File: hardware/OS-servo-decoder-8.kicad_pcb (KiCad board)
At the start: 2 copper layers, 41 x 74.5 mm, 59 parts, among them J1001 Conn_02x03_Odd_Even, J101 Screw_Terminal_01x04, J201 ICSP, J701 Conn_02x03_Odd_Even, J801 Conn_02x03_Odd_Even, J901 Conn_02x03_Odd_Even, SW601 SW_Push, SW602 SW_Push, SW603 SW_Push, SW604 SW_Push, SW605 SW_Push, U1001 6N137, U202 ATmega328-A, U901 MT2499A, Y201 Crystal_GND2

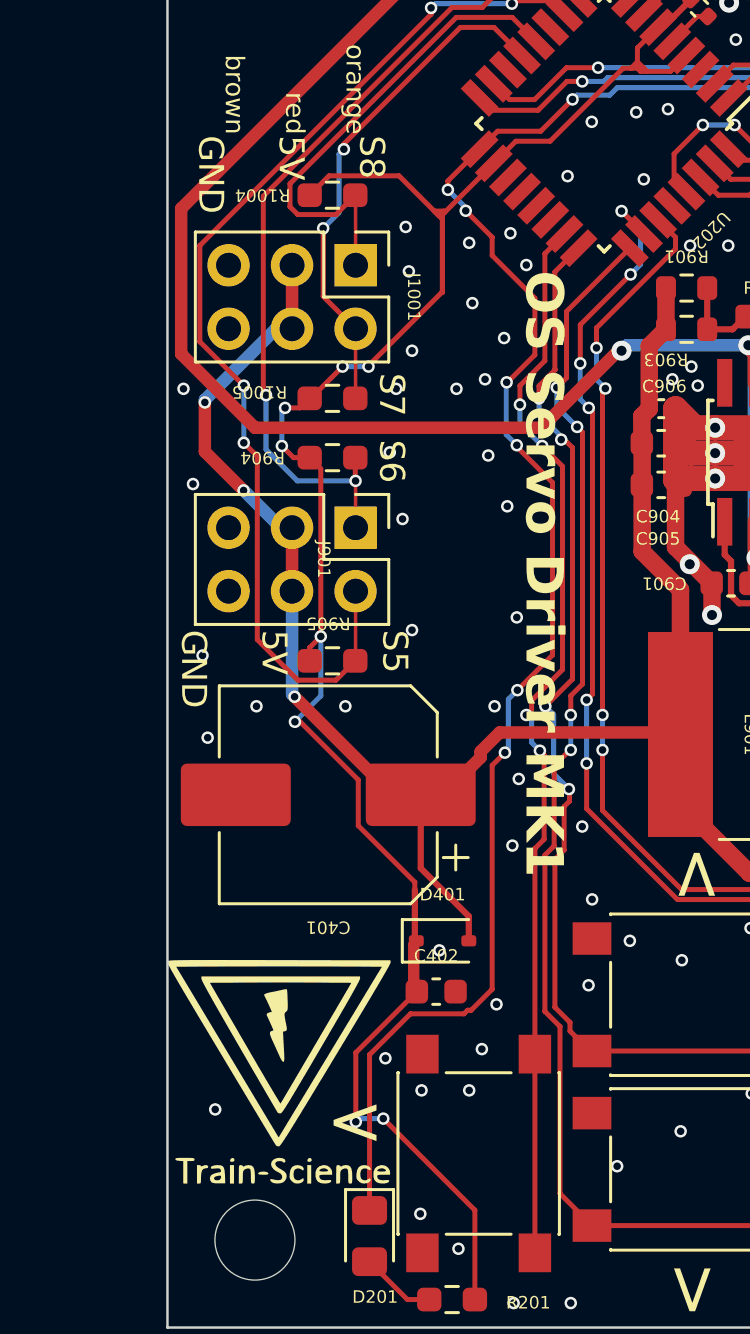
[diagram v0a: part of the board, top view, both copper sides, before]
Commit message: deleted source code in favor of sub module
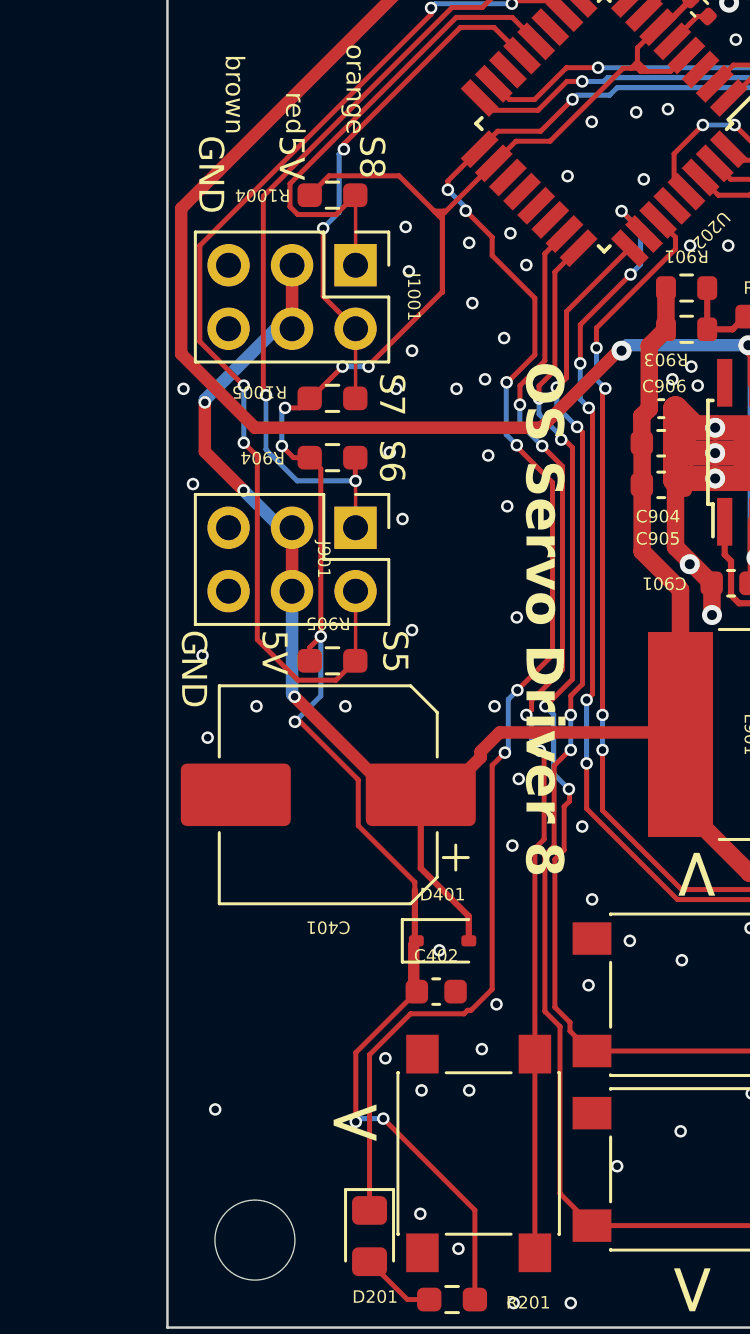
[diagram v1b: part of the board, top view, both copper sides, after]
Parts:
- removed G*** (x2): LOGO, custom_kicad_lib_sk:Train-Science logo small
- removed G***: LOGO, custom_kicad_lib_sk:servoDriverQR
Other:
- board text added: "OS Servo Driver 8"
- board text removed: "OS Servo Driver MK1"

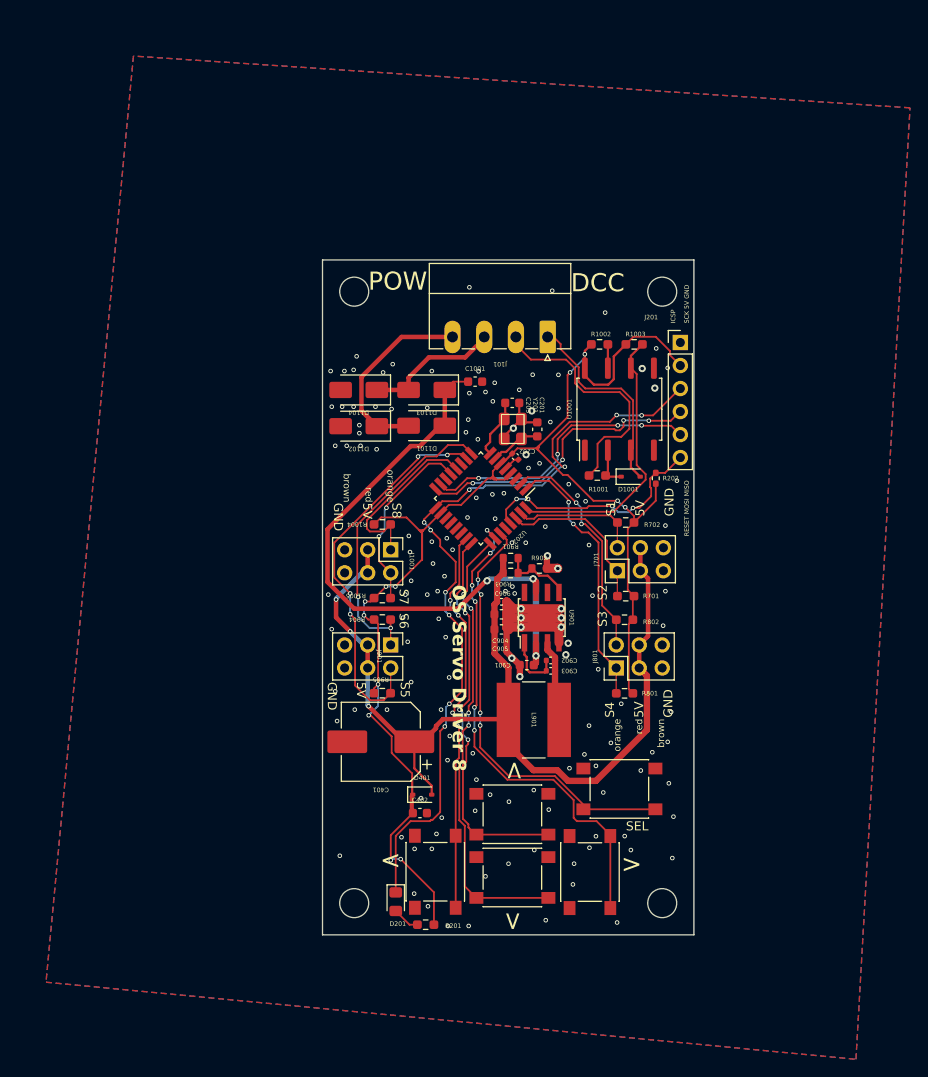
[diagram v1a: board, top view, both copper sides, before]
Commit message: update board file, made similar to OS solenoid decoder
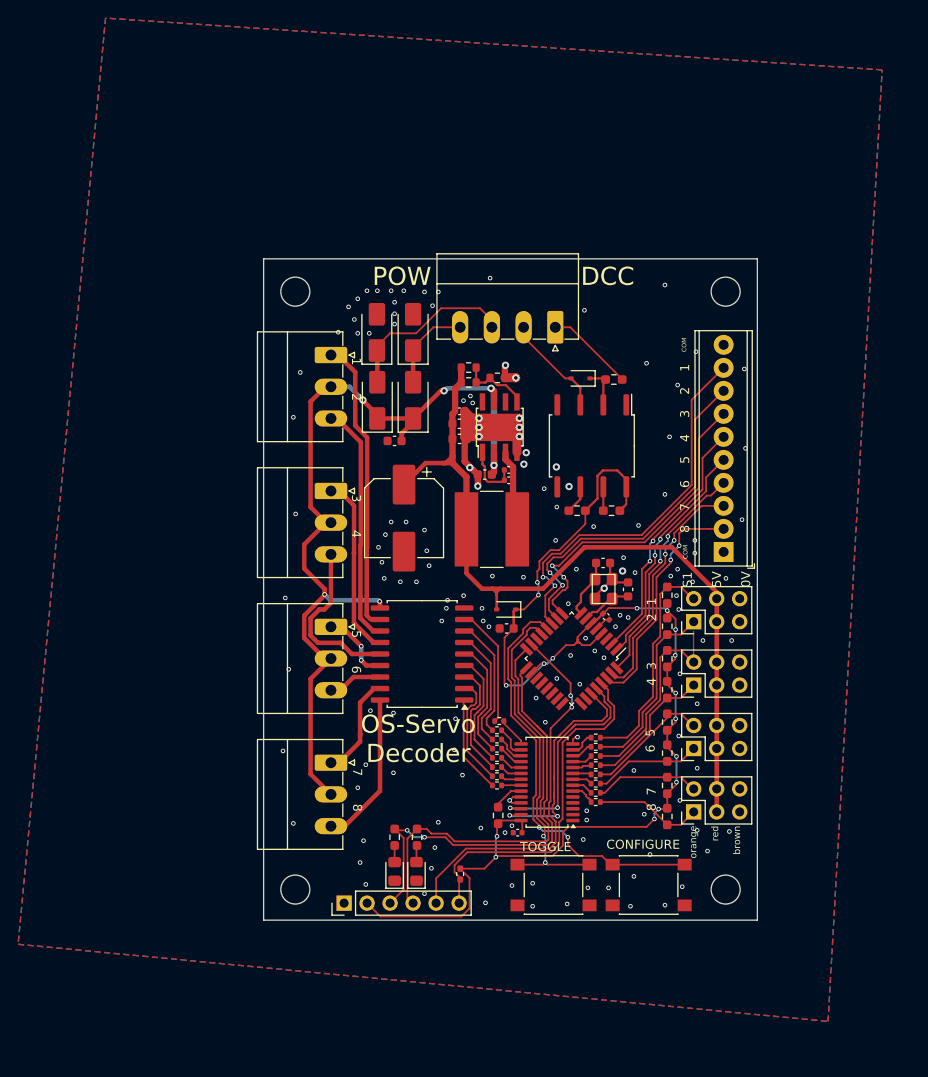
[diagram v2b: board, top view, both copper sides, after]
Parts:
- removed C1001: 100nF, Capacitor_SMD:C_0603_1608Metric
- removed the REF** at (104.0, 172.5)
- removed the REF** at (138.0, 172.5)
- removed the REF** at (138.0, 105.0)
- removed the REF** at (104.0, 105.0)
- removed the REF** at (120.9, 158.5)
- removed SW603, SW604, SW605: SW_Push, custom_kicad_lib_sk:tactile_SMD_6mm
- added C1601: 100nF, Capacitor_SMD:C_0402_1005Metric, F.Cu at (122.0, 164.7)
- added C501: 100nF, Capacitor_SMD:C_0603_1608Metric, F.Cu at (108.5, 121.5)
- added D202: LED, LED_SMD:LED_0805_2012Metric_Pad1.15x1.40mm_HandSolder, F.Cu at (110.9, 169.0)
- added G***: LOGO, custom_kicad_lib_sk:OS-model-railway-electronics-30mm, B.Cu at (121.3, 139.2)
- added J1301: Screw_Terminal_01x03, Connector_Phoenix_MC:PhoenixContact_MC_1,5_3-G-3.5_1x03_P3.50mm_Horizontal, F.Cu at (101.4, 112.0)
- added J1401: Screw_Terminal_01x03, Connector_Phoenix_MC:PhoenixContact_MC_1,5_3-G-3.5_1x03_P3.50mm_Horizontal, F.Cu at (101.4, 142.0)
- added J1501: Screw_Terminal_01x03, Connector_Phoenix_MC:PhoenixContact_MC_1,5_3-G-3.5_1x03_P3.50mm_Horizontal, F.Cu at (101.4, 157.0)
- added J401: Screw_Terminal_01x03, Connector_Phoenix_MC:PhoenixContact_MC_1,5_3-G-3.5_1x03_P3.50mm_Horizontal, F.Cu at (101.4, 127.0)
- added J501: Screw_Terminal_01x10, TerminalBlock_Phoenix:TerminalBlock_Phoenix_MPT-0,5-10-2.54_1x10_P2.54mm_Horizontal, F.Cu at (144.8, 133.7)
- added R1601: 10k, custom_kicad_lib_sk:R_0603_smalltext, F.Cu at (119.9, 162.8)
- added R1602: 220R, Resistor_SMD:R_0402_1005Metric, F.Cu at (130.7, 161.3)
- added R1603: 220R, Resistor_SMD:R_0402_1005Metric, F.Cu at (130.7, 160.3)
- added R1604: 220R, Resistor_SMD:R_0402_1005Metric, F.Cu at (130.7, 159.3)
- added R1605: 220R, Resistor_SMD:R_0402_1005Metric, F.Cu at (130.7, 158.3)
- added R1606: 220R, Resistor_SMD:R_0402_1005Metric, F.Cu at (130.7, 157.3)
- added R1607: 220R, Resistor_SMD:R_0402_1005Metric, F.Cu at (130.7, 156.3)
- added R1608: 220R, Resistor_SMD:R_0402_1005Metric, F.Cu at (130.7, 155.2)
- added R1609: 220R, Resistor_SMD:R_0402_1005Metric, F.Cu at (130.7, 154.2)
- added R1610: 220R, Resistor_SMD:R_0402_1005Metric, F.Cu at (120.0, 152.4)
- added R1611: 220R, Resistor_SMD:R_0402_1005Metric, F.Cu at (119.8, 153.4)
- added R1612: 220R, Resistor_SMD:R_0402_1005Metric, F.Cu at (119.8, 154.4)
- added R1613: 220R, Resistor_SMD:R_0402_1005Metric, F.Cu at (119.8, 155.4)
- added R1614: 220R, Resistor_SMD:R_0402_1005Metric, F.Cu at (119.8, 156.5)
- added R1615: 220R, Resistor_SMD:R_0402_1005Metric, F.Cu at (119.8, 157.5)
- added R1616: 220R, Resistor_SMD:R_0402_1005Metric, F.Cu at (119.8, 158.5)
- added R1617: 220R, Resistor_SMD:R_0402_1005Metric, F.Cu at (119.8, 159.5)
- added R203: 6k2, Resistor_SMD:R_0603_1608Metric_Pad0.98x0.95mm_HandSolder, F.Cu at (110.9, 165.2)
- added REF**: MountingHole_3.2mm_M3, MountingHole:MountingHole_3.2mm_M3, F.Cu at (145.0, 171.0)
- added REF**: MountingHole_3.2mm_M3, MountingHole:MountingHole_3.2mm_M3, F.Cu at (97.5, 105.0)
- added REF**: MountingHole_3.2mm_M3, MountingHole:MountingHole_3.2mm_M3, F.Cu at (97.5, 171.0)
- added REF**: MountingHole_3.2mm_M3, MountingHole:MountingHole_3.2mm_M3, F.Cu at (145.0, 105.0)
- added U1101: ULN2803A, Package_SO:SOIC-18W_7.5x11.6mm_P1.27mm, F.Cu at (111.5, 145.0)
- added U1601: PCA9685PW, Package_SO:TSSOP-28_4.4x9.7mm_P0.65mm, F.Cu at (125.3, 159.2)
- J101: value Screw_Terminal_01x04 -> FEMALE
- moved J201 72.2 mm to (102.9, 172.5), turned to 90 degrees
- moved R202 48.7 mm to (115.7, 169.3), turned to 90 degrees
- moved R1004 45.0 mm to (138.6, 162.9), turned to 90 degrees
- moved J1001 44.2 mm to (141.5, 162.4), turned to 90 degrees
- moved R1005 37.6 mm to (138.6, 159.5), turned to -90 degrees
- moved J901 35.3 mm to (141.5, 155.4), turned to 90 degrees
- moved R904 34.7 mm to (138.6, 155.9), turned to 90 degrees
- moved R905 31.6 mm to (138.6, 152.5), turned to -90 degrees
- moved C401 24.8 mm to (109.5, 130.0), turned to -90 degrees
- moved C402 22.5 mm to (120.8, 142.2), turned to 180 degrees
- moved D401 22.5 mm to (120.8, 140.1), turned to 180 degrees
- moved C901 21.5 mm to (118.4, 125.2)
- moved C904 21.5 mm to (115.6, 119.6)
- moved R902 21.5 mm to (119.8, 114.5)
- moved C903 21.5 mm to (121.1, 125.8)
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- renumbered D1103 to D501, D1104 to D502, D1101 to D503, D1102 to D504
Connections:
- net /atmega/MISO renamed /atmega/LED2
- D1001 pad 2: /DCC/DCC_B -> /Connector/A
- D201 pad 1: /atmega/LED -> GND
- D501 pad 2: /D_bridge/AC_2 -> /Buck/B
- D502 pad 1: /D_bridge/AC_2 -> /Buck/B
- D503 pad 2: /D_bridge/AC_1 -> /Buck/A
- D504 pad 1: /D_bridge/AC_1 -> /Buck/A
- J1001 pad 1: /atmega/bus4.pin1 -> /PCA9685/bus4.pin1
- J1001 pad 2: /atmega/bus4.pin2 -> /PCA9685/bus4.pin2
- J101 pad 1: /DCC/DCC_B -> /Connector/B
- J101 pad 2: /DCC/DCC_A -> /Connector/A
- J101 pad 3: /D_bridge/AC_2 -> /Buck/A
- J101 pad 4: /D_bridge/AC_1 -> /Buck/B
- J701 pad 1: /atmega/bus1.pin1 -> /PCA9685/bus1.pin1
- J701 pad 2: /atmega/bus1.pin2 -> /PCA9685/bus1.pin2
- J801 pad 1: /atmega/bus2.pin1 -> /PCA9685/bus2.pin1
- J801 pad 2: /atmega/bus2.pin2 -> /PCA9685/bus2.pin2
- J901 pad 1: /atmega/bus3.pin1 -> /PCA9685/bus3.pin1
- J901 pad 2: /atmega/bus3.pin2 -> /PCA9685/bus3.pin2
- R1001 pad 1: /DCC/DCC_A -> /Connector/B
- R1004 pad 1: /atmega/bus4.pin1 -> /PCA9685/bus4.pin1
- R1005 pad 1: /atmega/bus4.pin2 -> /PCA9685/bus4.pin2
- R201 pad 1: +5V -> /atmega/LED
- R701 pad 1: /atmega/bus1.pin1 -> /PCA9685/bus1.pin1
- R702 pad 1: /atmega/bus1.pin2 -> /PCA9685/bus1.pin2
- R801 pad 1: /atmega/bus2.pin1 -> /PCA9685/bus2.pin1
- R802 pad 1: /atmega/bus2.pin2 -> /PCA9685/bus2.pin2
- R904 pad 1: /atmega/bus3.pin1 -> /PCA9685/bus3.pin1
- R905 pad 1: /atmega/bus3.pin2 -> /PCA9685/bus3.pin2
- SW601 pad 2: /atmega/sw1 -> /atmega/toggle
- SW602 pad 2: /atmega/sw2 -> /atmega/conf
- U1001 pad 3: /DCC/DCC_B -> /Connector/A
- U202 pad 1: /atmega/bus2.pin1 -> /atmega/sw5
- U202 pad 10: /atmega/bus3.pin2 -> /atmega/sw2
- U202 pad 11: unconnected-(U202-PD7-Pad11) -> /atmega/sw1
- U202 pad 12: /atmega/bus4.pin1 -> /atmega/conf
- U202 pad 13: /atmega/bus4.pin2 -> /atmega/toggle
- U202 pad 2: /atmega/bus2.pin2 -> /atmega/sw4
- U202 pad 23: /atmega/sw1 -> unconnected-(U202-PC0-Pad23)
- U202 pad 24: /atmega/sw2 -> unconnected-(U202-PC1-Pad24)
- U202 pad 25: /atmega/sw3 -> unconnected-(U202-PC2-Pad25)
- U202 pad 26: /atmega/sw4 -> unconnected-(U202-PC3-Pad26)
- U202 pad 27: /atmega/sw5 -> /PCA9685/SDA
- U202 pad 28: unconnected-(U202-PC5-Pad28) -> /PCA9685/SCL
- U202 pad 30: /atmega/bus1.pin1 -> /atmega/sw8
- U202 pad 31: /atmega/bus1.pin2 -> /atmega/sw7
- U202 pad 32: /DCC/DCC_TTL -> /atmega/sw6
- U202 pad 9: /atmega/bus3.pin1 -> /atmega/sw3
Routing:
- net /atmega/conf: track 0.00 -> 45.7 mm, vias 0 -> 2
- net /atmega/bus3.pin2: track 42.7 -> 0.00 mm, vias 4 -> 0
- net /atmega/toggle: track 0.00 -> 39.0 mm, vias 0 -> 2
- net /atmega/LED: track 86.4 -> 49.5 mm, vias 10 -> 2
- net /atmega/bus3.pin1: track 33.7 -> 0.00 mm, vias 2 -> 0
- net /ULN2803/1.pin2: track 0.00 -> 32.5 mm
- net VCC: track 68.0 -> 98.2 mm, vias 3 -> 6
- net /atmega/bus2.pin1: track 29.8 -> 0.00 mm, vias 2 -> 0
- net /DCC/DCC_A: track 28.0 -> 0.00 mm
- net /DCC/DCC_TTL: track 30.4 -> 3.16 mm
- net /atmega/sw4: track 54.9 -> 28.0 mm, vias 6 -> 2
- net /ULN2803/1.pin1: track 0.00 -> 26.6 mm
- net /atmega/sw7: track 0.00 -> 26.5 mm, vias 0 -> 2
- net /PCA9685/SDA: track 0.00 -> 26.3 mm, vias 0 -> 2
- net /atmega/sw8: track 0.00 -> 26.2 mm, vias 0 -> 2
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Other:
- board size 41 x 74.5 mm -> 54.5 x 73 mm
- board text added: "1"
- board text added: "1 2"
- board text added: "2"
- board text added: "2 1"
- board text added: "3"
- board text added: "3 4"
- board text added: "4"
- board text added: "4 3"
- board text added: "5"
- board text added: "5 6"
- board text added: "6"
- board text added: "6 5"
- board text added: "7"
- board text added: "7 8"
- board text added: "8"
- board text added: "8 7"
- board text added: "COM"
- board text added: "CONFIGURE"
- board text added: "OS-Servo Decoder"
- board text added: "S1 5V 0V"
- board text added: "TOGGLE"
- board text added: "github.com/Open-Source-Model-Railway-Electronics/"
- board text removed: "<"
- board text removed: "ICSP"
- board text removed: "OS Servo Driver 8"
- board text removed: "RESET MOSI MISO"
- board text removed: "S1 5V GND"
- board text removed: "S2"
- board text removed: "S3"
- board text removed: "S4 5V GND"
- board text removed: "S5 5V GND"
- board text removed: "S6"
- board text removed: "S7"
- board text removed: "S8 5V GND"
- board text removed: "SCK 5V GND"
- board text removed: "SEL"

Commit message: added manual and picture
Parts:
- added D505: LED, LED_SMD:LED_0805_2012Metric_Pad1.15x1.40mm_HandSolder, F.Cu at (139.3, 113.3)
- added D506: LED, LED_SMD:LED_0805_2012Metric_Pad1.15x1.40mm_HandSolder, F.Cu at (139.3, 115.8)
- added D507: LED, LED_SMD:LED_0805_2012Metric_Pad1.15x1.40mm_HandSolder, F.Cu at (139.3, 118.4)
- added D508: LED, LED_SMD:LED_0805_2012Metric_Pad1.15x1.40mm_HandSolder, F.Cu at (139.3, 120.9)
- added D509: LED, LED_SMD:LED_0805_2012Metric_Pad1.15x1.40mm_HandSolder, F.Cu at (139.3, 123.4)
- added D510: LED, LED_SMD:LED_0805_2012Metric_Pad1.15x1.40mm_HandSolder, F.Cu at (139.3, 126.0)
- added D511: LED, LED_SMD:LED_0805_2012Metric_Pad1.15x1.40mm_HandSolder, F.Cu at (139.3, 128.5)
- added D512: LED, LED_SMD:LED_0805_2012Metric_Pad1.15x1.40mm_HandSolder, F.Cu at (139.4, 131.1)
- added R501: 1k, custom_kicad_lib_sk:R_0603_smalltext, F.Cu at (135.7, 113.5)
- added R502: 1k, custom_kicad_lib_sk:R_0603_smalltext, F.Cu at (135.7, 116.0)
- added R503: 1k, custom_kicad_lib_sk:R_0603_smalltext, F.Cu at (135.7, 118.5)
- added R504: 1k, custom_kicad_lib_sk:R_0603_smalltext, F.Cu at (135.7, 121.0)
- added R505: 1k, custom_kicad_lib_sk:R_0603_smalltext, F.Cu at (135.7, 123.5)
- added R506: 1k, custom_kicad_lib_sk:R_0603_smalltext, F.Cu at (135.7, 126.0)
- added R507: 1k, custom_kicad_lib_sk:R_0603_smalltext, F.Cu at (135.7, 128.6)
- added R508: 1k, custom_kicad_lib_sk:R_0603_smalltext, F.Cu at (135.7, 131.1)
- moved R1002 1.62 mm to (130.8, 128.9)
- moved R1003 1.62 mm to (127.0, 128.9)
- moved D1001 1.62 mm to (127.4, 114.3)
- moved U1001 1.62 mm to (128.6, 121.7)
- moved R1001 1.62 mm to (131.1, 114.4)
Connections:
- U202 pad 26: unconnected-(U202-PC3-Pad26) -> /atmega/sw6
- U202 pad 32: /atmega/sw6 -> /DCC/DCC_TTL
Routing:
- net /DCC/DCC_TTL: track 3.16 -> 25.3 mm, vias 0 -> 4
- net +5V: track 142.2 -> 161.9 mm
- net /atmega/sw6: track 25.6 -> 40.1 mm, vias 2 -> 5
- net /atmega/sw3: track 36.3 -> 41.9 mm, vias 2 -> 3
- net /atmega/sw2: track 39.5 -> 45.1 mm, vias 2 -> 3
- net /atmega/sw1: track 42.6 -> 47.9 mm, vias 2 -> 3
- net /atmega/sw4: track 28.0 -> 33.0 mm, vias 2 -> 1
- net /atmega/sw5: track 25.9 -> 30.9 mm, vias 2 -> 1
- net /atmega/sw7: track 26.5 -> 30.2 mm, vias 2 -> 1
- net /atmega/sw8: track 26.2 -> 29.8 mm, vias 2 -> 1
- net /PCA9685/bus2.pin2: track 22.2 -> 19.4 mm
- net Net-(D512-A): track 0.00 -> 1.76 mm
- net Net-(D505-A): track 0.00 -> 1.73 mm
- net Net-(D506-A): track 0.00 -> 1.71 mm
- net Net-(D507-A): track 0.00 -> 1.70 mm
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
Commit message: added translations
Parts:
- removed D505, D506, D507, D508, D509, D510, D511, D512: LED, LED_SMD:LED_0805_2012Metric_Pad1.15x1.40mm_HandSolder
- removed J501: Screw_Terminal_01x10, TerminalBlock_Phoenix:TerminalBlock_Phoenix_MPT-0,5-10-2.54_1x10_P2.54mm_Horizontal
- removed R501, R502, R503, R504, R505, R506, R507, R508: 1k, custom_kicad_lib_sk:R_0603_smalltext
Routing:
- net /atmega/sw1: track 47.9 -> 0.00 mm, vias 3 -> 0
- net /atmega/sw2: track 45.1 -> 0.00 mm, vias 3 -> 0
- net /atmega/sw3: track 41.9 -> 0.00 mm, vias 3 -> 0
- net /atmega/sw6: track 40.1 -> 0.00 mm, vias 5 -> 0
- net /atmega/sw4: track 33.0 -> 0.00 mm, vias 1 -> 0
- net /atmega/sw5: track 30.9 -> 0.00 mm, vias 1 -> 0
- net /atmega/sw7: track 30.2 -> 0.00 mm, vias 1 -> 0
- net /atmega/sw8: track 29.8 -> 0.00 mm, vias 1 -> 0
- net +5V: track 161.9 -> 141.2 mm
- net +5VA: track 91.3 -> 84.3 mm
- net VCC: track 98.2 -> 95.0 mm
- net Net-(D512-A): track 1.76 -> 0.00 mm
- net Net-(D505-A): track 1.73 -> 0.00 mm
- net Net-(D506-A): track 1.71 -> 0.00 mm
- net Net-(D507-A): track 1.70 -> 0.00 mm
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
